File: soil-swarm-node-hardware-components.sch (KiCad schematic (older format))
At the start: 50 parts, among them J1 Conn_ARM_JTAG_SWD_10, J3 BATT_CONN, J4 USB_B_Micro, Q1 DMP3099L-13, Q2 Q_NMOS_GSD, Q3 DMP3099L-13, U3 MCP73812T-420I-OT, X1 32MHz, X2 32,768kHz

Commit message: finalizing 2.0.0
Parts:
- C1, C15, C2, C22, C24, C5: value 100nF -> 100n
- C10, C16, C17, C18: value 4,7µF -> 4.7u
- C11, C7: value 1pF -> 1p
- C12: value 100pF -> 100p
- C13, C14, C19, C20: value 12pF -> 12p
- C21: value 10µF -> 10u
- C23: value 10nF -> 10n
- C3: value 820pF -> 820p
- C6, C8: value 1µF -> 1u
- C9: value 47nF -> 47n
- L1: value 15nH -> 15n
- L2, L4: value 10µH -> 10u
- L3: value 3,9nH -> 3.9n
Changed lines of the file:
@@
 EESchema Schematic File Version 4
-LIBS:power
-LIBS:74xx
 LIBS:soil-swarm-node-hardware-cache
 EELAYER 26 0
@@
 AR Path="/5CDC06D0/5CDCBFD7" Ref="C13"  Part="1"
 F 0 "C13" V 4652 1050 50  0000 C CNN
-F 1 "12pF" V 4561 1050 50  0000 C CNN
+F 1 "12p" V 4561 1050 50  0000 C CNN
 F 2 "Capacitor_SMD:C_0402_1005Metric" H 4438 900 50  0001 C CNN
 F 3 "~" H 4400 1050 50  0001 C CNN
@@
 AR Path="/5CDC06D0/5CDCBFDE" Ref="C14"  Part="1"
 F 0 "C14" V 4652 1450 50  0000 C CNN
-F 1 "12pF" V 4561 1450 50  0000 C CNN
+F 1 "12p" V 4561 1450 50  0000 C CNN
 F 2 "Capacitor_SMD:C_0402_1005Metric" H 4438 1300 50  0001 C CNN
 F 3 "~" H 4400 1450 50  0001 C CNN
@@
 AR Path="/5CDC06D0/5CDCEF68" Ref="C10"  Part="1"
 F 0 "C10" H 8315 1246 50  0000 L CNN
-F 1 "4,7µF" H 8315 1155 50  0000 L CNN
+F 1 "4.7u" H 8315 1155 50  0000 L CNN
 F 2 "Capacitor_SMD:C_0402_1005Metric" H 8238 1050 50  0001 C CNN
 F 3 "~" H 8200 1200 50  0001 C CNN
@@
 AR Path="/5CDC06D0/5CDCEF75" Ref="L1"  Part="1"
 F 0 "L1" H 1753 3746 50  0000 L CNN
-F 1 "15nH" H 1753 3655 50  0000 L CNN
+F 1 "15n" H 1753 3655 50  0000 L CNN
 F 2 "Inductor_SMD:L_0603_1608Metric" H 1700 3700 50  0001 C CNN
 F 3 "~" H 1700 3700 50  0001 C CNN
@@
 AR Path="/5CDC06D0/5CDCEF7C" Ref="L2"  Part="1"
 F 0 "L2" H 1753 4046 50  0000 L CNN
-F 1 "10µH" H 1753 3955 50  0000 L CNN
+F 1 "10u" H 1753 3955 50  0000 L CNN
 F 2 "Inductor_SMD:L_0603_1608Metric" H 1700 4000 50  0001 C CNN
 F 3 "~" H 1700 4000 50  0001 C CNN
@@
 AR Path="/5CDC06D0/5CDCEF8A" Ref="C6"  Part="1"
 F 0 "C6" H 1815 4346 50  0000 L CNN
-F 1 "1µF" H 1815 4255 50  0000 L CNN
+F 1 "1u" H 1815 4255 50  0000 L CNN
 F 2 "Capacitor_SMD:C_0402_1005Metric" H 1738 4150 50  0001 C CNN
 F 3 "~" H 1700 4300 50  0001 C CNN
@@
 AR Path="/5CDC06D0/5CDCEF93" Ref="C9"  Part="1"
 F 0 "C9" H 2215 4346 50  0000 L CNN
-F 1 "47nF" H 2215 4255 50  0000 L CNN
+F 1 "47n" H 2215 4255 50  0000 L CNN
 F 2 "Capacitor_SMD:C_0402_1005Metric" H 2138 4150 50  0001 C CNN
 F 3 "~" H 2100 4300 50  0001 C CNN
@@
 AR Path="/5CDC06D0/5CDCEFA5" Ref="C15"  Part="1"
 F 0 "C15" H 3465 3946 50  0000 L CNN
-F 1 "100nF" H 3465 3855 50  0000 L CNN
+F 1 "100n" H 3465 3855 50  0000 L CNN
 F 2 "Capacitor_SMD:C_0402_1005Metric" H 3388 3750 50  0001 C CNN
 F 3 "~" H 3350 3900 50  0001 C CNN
@@
 AR Path="/5CDC06D0/5CDCEFB2" Ref="C12"  Part="1"
 F 0 "C12" H 2865 3946 50  0000 L CNN
-F 1 "100pF" H 2865 3855 50  0000 L CNN
+F 1 "100p" H 2865 3855 50  0000 L CNN
 F 2 "Capacitor_SMD:C_0402_1005Metric" H 2788 3750 50  0001 C CNN
 F 3 "~" H 2750 3900 50  0001 C CNN
@@
 AR Path="/5CDC06D0/5CDCEFC1" Ref="C3"  Part="1"
 F 0 "C3" H 1165 3696 50  0000 L CNN
-F 1 "820pF" H 1165 3605 50  0000 L CNN
+F 1 "820p" H 1165 3605 50  0000 L CNN
 F 2 "Capacitor_SMD:C_0402_1005Metric" H 1088 3500 50  0001 C CNN
 F 3 "~" H 1050 3650 50  0001 C CNN
@@
 AR Path="/5CDC06D0/5CDCEFD8" Ref="C11"  Part="1"
 F 0 "C11" H 2515 5596 50  0000 L CNN
-F 1 "1pF" H 2515 5505 50  0000 L CNN
+F 1 "1p" H 2515 5505 50  0000 L CNN
 F 2 "Capacitor_SMD:C_0402_1005Metric" H 2438 5400 50  0001 C CNN
 F 3 "~" H 2400 5550 50  0001 C CNN
@@
 AR Path="/5CDC06D0/5CDCEFDF" Ref="C7"  Part="1"
 F 0 "C7" H 1815 5596 50  0000 L CNN
-F 1 "1pF" H 1815 5505 50  0000 L CNN
+F 1 "1p" H 1815 5505 50  0000 L CNN
 F 2 "Capacitor_SMD:C_0402_1005Metric" H 1738 5400 50  0001 C CNN
 F 3 "~" H 1700 5550 50  0001 C CNN
@@
 AR Path="/5CDC06D0/5CDCEFE6" Ref="L3"  Part="1"
 F 0 "L3" V 2240 5400 50  0000 C CNN
-F 1 "3,9nH" V 2149 5400 50  0000 C CNN
+F 1 "3.9n" V 2149 5400 50  0000 C CNN
 F 2 "Inductor_SMD:L_0603_1608Metric" H 2050 5400 50  0001 C CNN
 F 3 "~" H 2050 5400 50  0001 C CNN
@@
 AR Path="/5CDC06D0/5CDCF006" Ref="C8"  Part="1"
 F 0 "C8" H 7915 1246 50  0000 L CNN
-F 1 "1µF" H 7915 1155 50  0000 L CNN
+F 1 "1u" H 7915 1155 50  0000 L CNN
 F 2 "Capacitor_SMD:C_0402_1005Metric" H 7838 1050 50  0001 C CNN
 F 3 "~" H 7800 1200 50  0001 C CNN
@@
 AR Path="/5CDC06D0/5CDCF00D" Ref="C5"  Part="1"
 F 0 "C5" H 7465 1246 50  0000 L CNN
-F 1 "100nF" H 7465 1155 50  0000 L CNN
+F 1 "100n" H 7465 1155 50  0000 L CNN
 F 2 "Capacitor_SMD:C_0402_1005Metric" H 7388 1050 50  0001 C CNN
 F 3 "~" H 7350 1200 50  0001 C CNN
@@
 AR Path="/5CDC06D0/5CDCF014" Ref="C2"  Part="1"
 F 0 "C2" H 7015 1246 50  0000 L CNN
-F 1 "100nF" H 7015 1155 50  0000 L CNN
+F 1 "100n" H 7015 1155 50  0000 L CNN
 F 2 "Capacitor_SMD:C_0402_1005Metric" H 6938 1050 50  0001 C CNN
 F 3 "~" H 6900 1200 50  0001 C CNN
@@
 AR Path="/5CDC06D0/5CDCF01B" Ref="C1"  Part="1"
 F 0 "C1" H 6515 1246 50  0000 L CNN
-F 1 "100nF" H 6515 1155 50  0000 L CNN
+F 1 "100n" H 6515 1155 50  0000 L CNN
 F 2 "Capacitor_SMD:C_0402_1005Metric" H 6438 1050 50  0001 C CNN
 F 3 "~" H 6400 1200 50  0001 C CNN
@@
 AR Path="/5CDC06D0/5CDD4281" Ref="L4"  Part="1"
 F 0 "L4" H 9050 1265 50  0000 C CNN
-F 1 "10µH" H 9050 1174 50  0000 C CNN
+F 1 "10u" H 9050 1174 50  0000 C CNN
 F 2 "Inductor_SMD:L_0603_1608Metric" H 9050 1050 50  0001 C CNN
 F 3 "~" H 9050 1050 50  0001 C CNN
@@
 AR Path="/5CDC06D0/5CDD4288" Ref="C17"  Part="1"
 F 0 "C17" H 6315 2146 50  0000 L CNN
-F 1 "4,7µF" H 6315 2055 50  0000 L CNN
+F 1 "4.7u" H 6315 2055 50  0000 L CNN
 F 2 "Capacitor_SMD:C_0402_1005Metric" H 6238 1950 50  0001 C CNN
 F 3 "~" H 6200 2100 50  0001 C CNN
@@
 AR Path="/5CDC06D0/5CDD429E" Ref="C16"  Part="1"
 F 0 "C16" H 7015 2046 50  0000 L CNN
-F 1 "4,7µF" H 7015 1955 50  0000 L CNN
+F 1 "4.7u" H 7015 1955 50  0000 L CNN
 F 2 "Capacitor_SMD:C_0402_1005Metric" H 6938 1850 50  0001 C CNN
 F 3 "~" H 6900 2000 50  0001 C CNN
@@
 AR Path="/5CDC06D0/5CDD42AB" Ref="C18"  Part="1"
 F 0 "C18" H 8365 2046 50  0000 L CNN
-F 1 "4,7µF" H 8365 1955 50  0000 L CNN
+F 1 "4.7u" H 8365 1955 50  0000 L CNN
 F 2 "Capacitor_SMD:C_0402_1005Metric" H 8288 1850 50  0001 C CNN
 F 3 "~" H 8250 2000 50  0001 C CNN
@@
 AR Path="/5CDC06D0/5CDDAEC5" Ref="C19"  Part="1"
 F 0 "C19" V 4202 2100 50  0000 C CNN
-F 1 "12pF" V 4111 2100 50  0000 C CNN
+F 1 "12p" V 4111 2100 50  0000 C CNN
 F 2 "Capacitor_SMD:C_0402_1005Metric" H 3988 1950 50  0001 C CNN
 F 3 "~" H 3950 2100 50  0001 C CNN
@@
 AR Path="/5CDC06D0/5CDDAECC" Ref="C20"  Part="1"
 F 0 "C20" V 4202 2500 50  0000 C CNN
-F 1 "12pF" V 4111 2500 50  0000 C CNN
+F 1 "12p" V 4111 2500 50  0000 C CNN
 F 2 "Capacitor_SMD:C_0402_1005Metric" H 3988 2350 50  0001 C CNN
 F 3 "~" H 3950 2500 50  0001 C CNN
@@
 AR Path="/5CDC06D0/5CDE0A07" Ref="C21"  Part="1"
 F 0 "C21" H 8915 4596 50  0000 L CNN
-F 1 "10µF" H 8915 4505 50  0000 L CNN
+F 1 "10u" H 8915 4505 50  0000 L CNN
 F 2 "Capacitor_SMD:C_0402_1005Metric" H 8838 4400 50  0001 C CNN
 F 3 "~" H 8800 4550 50  0001 C CNN
@@
 AR Path="/5CDC06D0/5CDE0A0E" Ref="C22"  Part="1"
 F 0 "C22" H 9315 4596 50  0000 L CNN
-F 1 "100nF" H 9315 4505 50  0000 L CNN
+F 1 "100n" H 9315 4505 50  0000 L CNN
 F 2 "Capacitor_SMD:C_0402_1005Metric" H 9238 4400 50  0001 C CNN
 F 3 "~" H 9200 4550 50  0001 C CNN
@@
 AR Path="/5CDC06D0/5CDE0A2F" Ref="C24"  Part="1"
 F 0 "C24" H 10315 3646 50  0000 L CNN
-F 1 "100nF" H 10315 3555 50  0000 L CNN
+F 1 "100n" H 10315 3555 50  0000 L CNN
 F 2 "Capacitor_SMD:C_0402_1005Metric" H 10238 3450 50  0001 C CNN
 F 3 "~" H 10200 3600 50  0001 C CNN
@@
 AR Path="/5CDC06D0/5CDE0A3E" Ref="C23"  Part="1"
 F 0 "C23" H 9815 3646 50  0000 L CNN
-F 1 "10nF" H 9815 3555 50  0000 L CNN
+F 1 "10n" H 9815 3555 50  0000 L CNN
 F 2 "Capacitor_SMD:C_0402_1005Metric" H 9738 3450 50  0001 C CNN
 F 3 "~" H 9700 3600 50  0001 C CNN

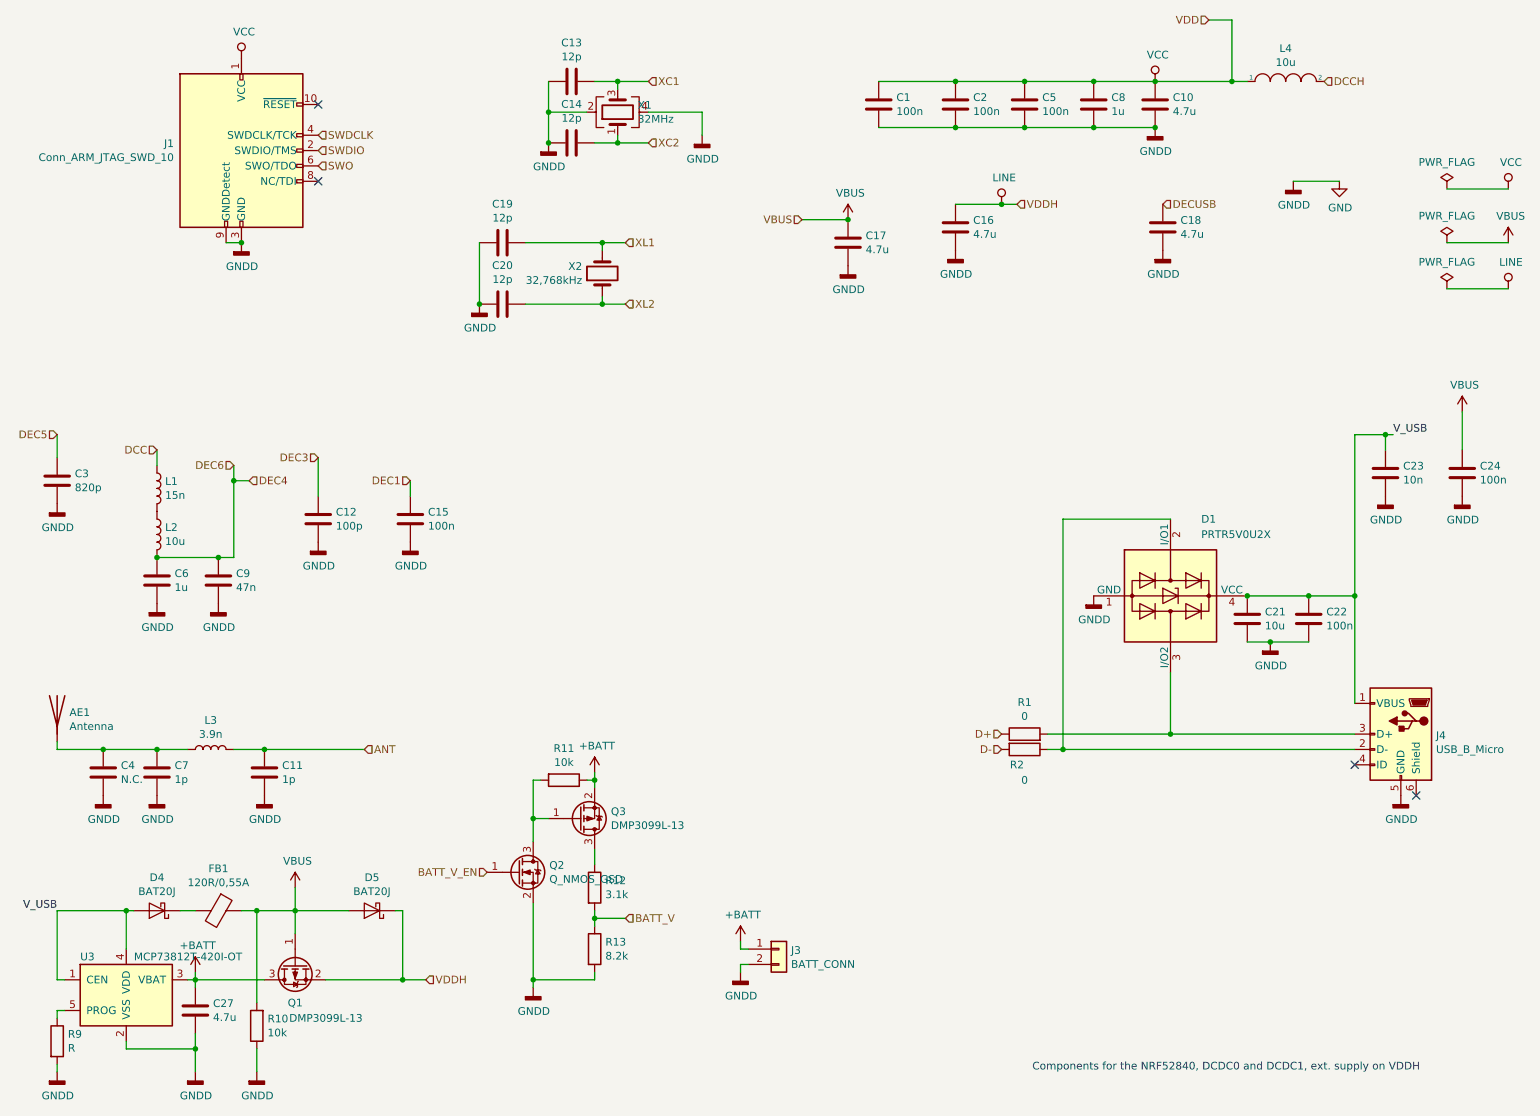
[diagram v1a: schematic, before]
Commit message: update based on Nordic specification
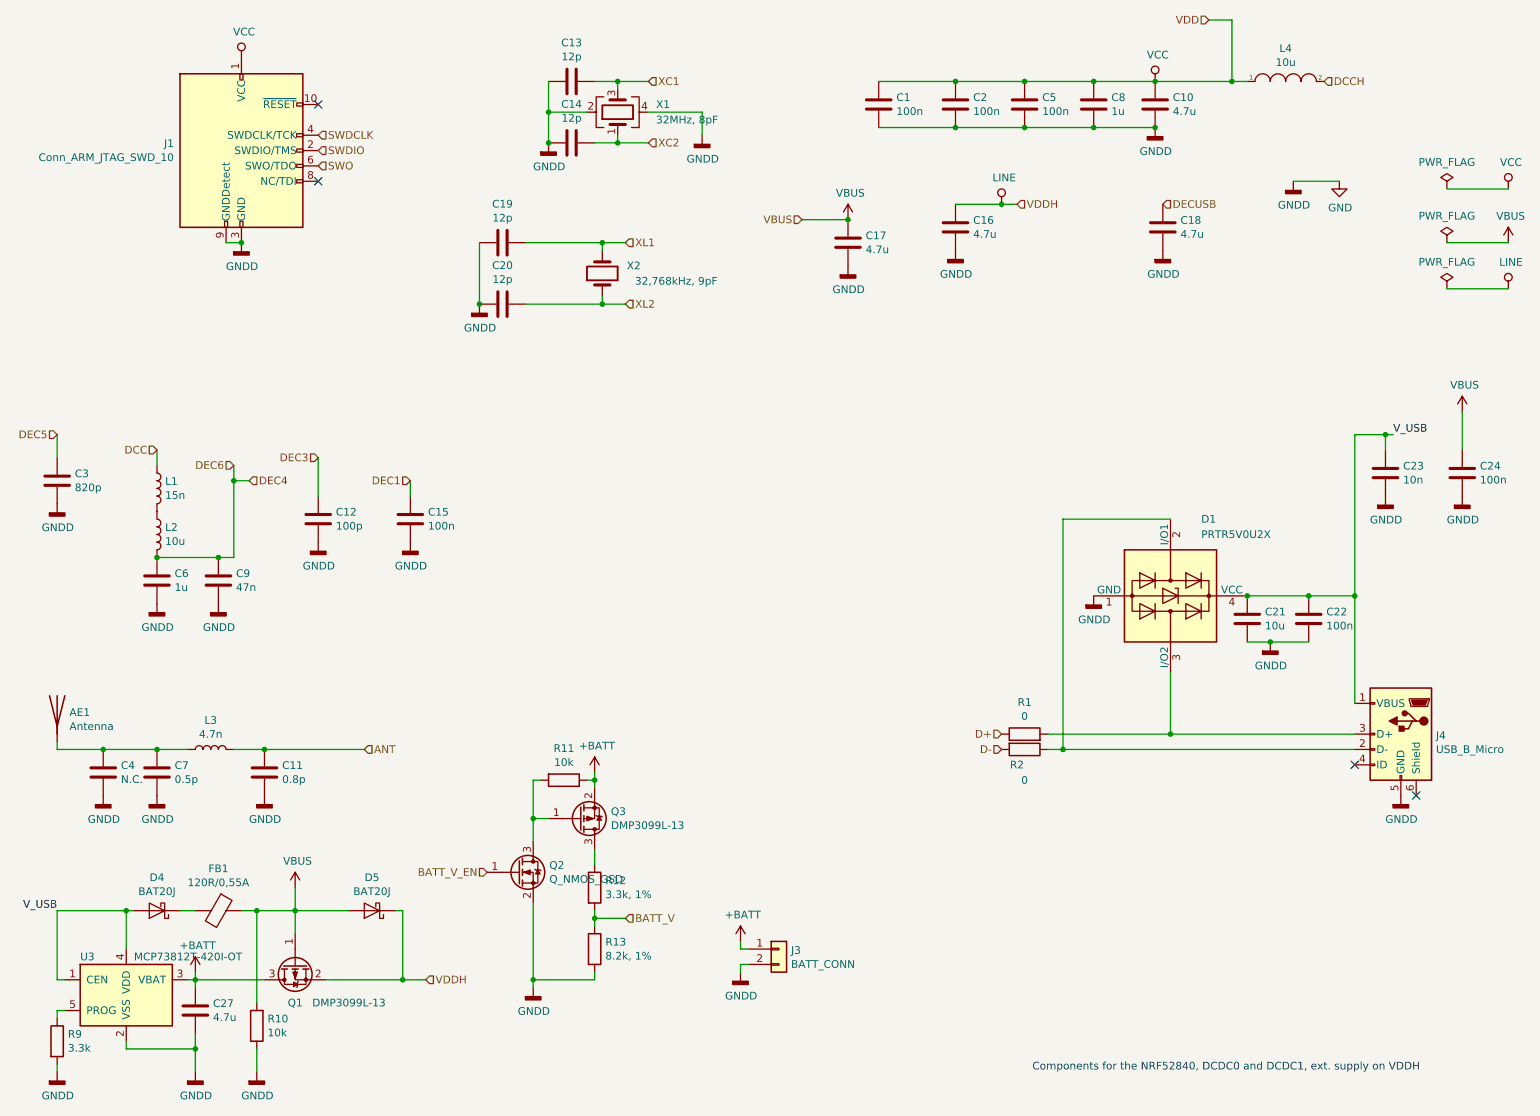
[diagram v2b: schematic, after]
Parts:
- C10, C16, C17, C18, C21, C27, C6, C8: footprint Capacitor_SMD:C_0402_1005Metric -> Capacitor_SMD:C_0603_1608Metric
- C11: value 1p -> 0.8p
- C7: value 1p -> 0.5p
- L1: footprint Inductor_SMD:L_0603_1608Metric -> Inductor_SMD:L_0402_1005Metric
- L3: value 3.9n -> 4.7n; footprint Inductor_SMD:L_0603_1608Metric -> Inductor_SMD:L_0402_1005Metric
- R12: value 3.1k -> 3.3k, 1%
- R13: value 8.2k -> 8.2k, 1%
- R9: value R -> 3.3k
- X1: value 32MHz -> 32MHz, 8pF; footprint Crystal:Crystal_SMD_3225-4Pin_3.2x2.5mm -> Crystal:Crystal_SMD_2016-4Pin_2.0x1.6mm
- X2: value 32,768kHz -> 32,768kHz, 9pF; footprint Crystal:Crystal_SMD_MicroCrystal_CC4V-T1A-2Pin_5.0x1.9mm -> Crystal:Crystal_SMD_3215-2Pin_3.2x1.5mm
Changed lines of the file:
@@
 AR Path="/5CDCBFE5" Ref="X?"  Part="1"
 AR Path="/5CDC06D0/5CDCBFE5" Ref="X1"  Part="1"
-F 0 "X1" V 4746 1119 50  0000 R CNN
-F 1 "32MHz" V 4655 1119 50  0000 R CNN
-F 2 "Crystal:Crystal_SMD_3225-4Pin_3.2x2.5mm" H 4700 1250 50  0001 C CNN
+F 0 "X1" V 4750 1000 50  0000 R CNN
+F 1 "32MHz, 8pF" V 4650 1000 50  0000 R CNN
+F 2 "Crystal:Crystal_SMD_2016-4Pin_2.0x1.6mm" H 4700 1250 50  0001 C CNN
 F 3 "~" H 4700 1250 50  0001 C CNN
 	1    4700 1250
@@
 F 0 "C10" H 8315 1246 50  0000 L CNN
 F 1 "4.7u" H 8315 1155 50  0000 L CNN
-F 2 "Capacitor_SMD:C_0402_1005Metric" H 8238 1050 50  0001 C CNN
+F 2 "Capacitor_SMD:C_0603_1608Metric" H 8238 1050 50  0001 C CNN
 F 3 "~" H 8200 1200 50  0001 C CNN
 	1    8200 1200
@@
 F 0 "L1" H 1753 3746 50  0000 L CNN
 F 1 "15n" H 1753 3655 50  0000 L CNN
-F 2 "Inductor_SMD:L_0603_1608Metric" H 1700 3700 50  0001 C CNN
+F 2 "Inductor_SMD:L_0402_1005Metric" H 1700 3700 50  0001 C CNN
 F 3 "~" H 1700 3700 50  0001 C CNN
 	1    1700 3700
@@
 F 0 "C6" H 1815 4346 50  0000 L CNN
 F 1 "1u" H 1815 4255 50  0000 L CNN
-F 2 "Capacitor_SMD:C_0402_1005Metric" H 1738 4150 50  0001 C CNN
+F 2 "Capacitor_SMD:C_0603_1608Metric" H 1738 4150 50  0001 C CNN
 F 3 "~" H 1700 4300 50  0001 C CNN
 	1    1700 4300
@@
 AR Path="/5CDC06D0/5CDCEFD8" Ref="C11"  Part="1"
 F 0 "C11" H 2515 5596 50  0000 L CNN
-F 1 "1p" H 2515 5505 50  0000 L CNN
+F 1 "0.8p" H 2515 5505 50  0000 L CNN
 F 2 "Capacitor_SMD:C_0402_1005Metric" H 2438 5400 50  0001 C CNN
 F 3 "~" H 2400 5550 50  0001 C CNN
@@
 AR Path="/5CDC06D0/5CDCEFDF" Ref="C7"  Part="1"
 F 0 "C7" H 1815 5596 50  0000 L CNN
-F 1 "1p" H 1815 5505 50  0000 L CNN
+F 1 "0.5p" H 1815 5505 50  0000 L CNN
 F 2 "Capacitor_SMD:C_0402_1005Metric" H 1738 5400 50  0001 C CNN
 F 3 "~" H 1700 5550 50  0001 C CNN
@@
 AR Path="/5CDC06D0/5CDCEFE6" Ref="L3"  Part="1"
 F 0 "L3" V 2240 5400 50  0000 C CNN
-F 1 "3.9n" V 2149 5400 50  0000 C CNN
-F 2 "Inductor_SMD:L_0603_1608Metric" H 2050 5400 50  0001 C CNN
+F 1 "4.7n" V 2149 5400 50  0000 C CNN
+F 2 "Inductor_SMD:L_0402_1005Metric" H 2050 5400 50  0001 C CNN
 F 3 "~" H 2050 5400 50  0001 C CNN
 	1    2050 5400
@@
 F 0 "C8" H 7915 1246 50  0000 L CNN
 F 1 "1u" H 7915 1155 50  0000 L CNN
-F 2 "Capacitor_SMD:C_0402_1005Metric" H 7838 1050 50  0001 C CNN
+F 2 "Capacitor_SMD:C_0603_1608Metric" H 7838 1050 50  0001 C CNN
 F 3 "~" H 7800 1200 50  0001 C CNN
 	1    7800 1200
@@
 F 0 "C17" H 6315 2146 50  0000 L CNN
 F 1 "4.7u" H 6315 2055 50  0000 L CNN
-F 2 "Capacitor_SMD:C_0402_1005Metric" H 6238 1950 50  0001 C CNN
+F 2 "Capacitor_SMD:C_0603_1608Metric" H 6238 1950 50  0001 C CNN
 F 3 "~" H 6200 2100 50  0001 C CNN
 	1    6200 2100
@@
 F 0 "C16" H 7015 2046 50  0000 L CNN
 F 1 "4.7u" H 7015 1955 50  0000 L CNN
-F 2 "Capacitor_SMD:C_0402_1005Metric" H 6938 1850 50  0001 C CNN
+F 2 "Capacitor_SMD:C_0603_1608Metric" H 6938 1850 50  0001 C CNN
 F 3 "~" H 6900 2000 50  0001 C CNN
 	1    6900 2000
@@
 F 0 "C18" H 8365 2046 50  0000 L CNN
 F 1 "4.7u" H 8365 1955 50  0000 L CNN
-F 2 "Capacitor_SMD:C_0402_1005Metric" H 8288 1850 50  0001 C CNN
+F 2 "Capacitor_SMD:C_0603_1608Metric" H 8288 1850 50  0001 C CNN
 F 3 "~" H 8250 2000 50  0001 C CNN
 	1    8250 2000
@@
 AR Path="/5CDDAED3" Ref="X?"  Part="1"
 AR Path="/5CDC06D0/5CDDAED3" Ref="X2"  Part="1"
-F 0 "X2" V 4646 2431 50  0000 L CNN
-F 1 "32,768kHz" V 4555 2431 50  0000 L CNN
-F 2 "Crystal:Crystal_SMD_MicroCrystal_CC4V-T1A-2Pin_5.0x1.9mm" H 4600 2300 50  0001 C CNN
+F 0 "X2" V 4650 2050 50  0000 L CNN
+F 1 "32,768kHz, 9pF" V 4550 1550 50  0000 L CNN
+F 2 "Crystal:Crystal_SMD_3215-2Pin_3.2x1.5mm" H 4600 2300 50  0001 C CNN
 F 3 "~" H 4600 2300 50  0001 C CNN
 	1    4600 2300
@@
 F 0 "C21" H 8915 4596 50  0000 L CNN
 F 1 "10u" H 8915 4505 50  0000 L CNN
-F 2 "Capacitor_SMD:C_0402_1005Metric" H 8838 4400 50  0001 C CNN
+F 2 "Capacitor_SMD:C_0603_1608Metric" H 8838 4400 50  0001 C CNN
 F 3 "~" H 8800 4550 50  0001 C CNN
 	1    8800 4550
@@
 F 0 "C27" H 2065 7146 50  0000 L CNN
 F 1 "4.7u" H 2065 7055 50  0000 L CNN
-F 2 "Capacitor_SMD:C_0402_1005Metric" H 1988 6950 50  0001 C CNN
+F 2 "Capacitor_SMD:C_0603_1608Metric" H 1988 6950 50  0001 C CNN
 F 3 "~" H 1950 7100 50  0001 C CNN
 	1    1950 7100
@@
 P 1050 7300
 F 0 "R9" H 1120 7346 50  0000 L CNN
-F 1 "R" H 1120 7255 50  0000 L CNN
+F 1 "3.3k" H 1120 7255 50  0000 L CNN
 F 2 "Resistor_SMD:R_0402_1005Metric" V 980 7300 50  0001 C CNN
 F 3 "~" H 1050 7300 50  0001 C CNN
@@
 P 2600 6800
 F 0 "Q1" V 2850 6800 50  0000 C CNN
-F 1 "DMP3099L-13" V 2950 6600 50  0000 C CNN
+F 1 "DMP3099L-13" V 2850 6450 50  0000 C CNN
 F 2 "Package_TO_SOT_SMD:SOT-23" H 2800 6900 50  0001 C CNN
 F 3 "~" H 2600 6800 50  0001 C CNN
@@
 P 4550 6300
 F 0 "R12" H 4620 6346 50  0000 L CNN
-F 1 "3.1k" H 4620 6255 50  0000 L CNN
+F 1 "3.3k, 1%" H 4620 6255 50  0000 L CNN
 F 2 "Resistor_SMD:R_0402_1005Metric" V 4480 6300 50  0001 C CNN
 F 3 "~" H 4550 6300 50  0001 C CNN
@@
 P 4550 6700
 F 0 "R13" H 4620 6746 50  0000 L CNN
-F 1 "8.2k" H 4620 6655 50  0000 L CNN
+F 1 "8.2k, 1%" H 4620 6655 50  0000 L CNN
 F 2 "Resistor_SMD:R_0402_1005Metric" V 4480 6700 50  0001 C CNN
 F 3 "~" H 4550 6700 50  0001 C CNN

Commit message: update schematic
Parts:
- D1: symbol Power_Protection:PRTR5V0U2X -> soil-swarm-node-hardware-rescue:PRTR5V0U2X-Power_Protection
- J1: symbol Connector:Conn_ARM_JTAG_SWD_10 -> soil-swarm-node-hardware-rescue:Conn_ARM_JTAG_SWD_10-Connector
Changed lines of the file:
@@
 $EndDescr
 $Comp
-L Connector:Conn_ARM_JTAG_SWD_10 J?
+L soil-swarm-node-hardware-rescue:Conn_ARM_JTAG_SWD_10-Connector J?
 U 1 1 5CDC6ACC
 P 2250 1500
@@
 $EndComp
 $Comp
-L Power_Protection:PRTR5V0U2X D?
+L soil-swarm-node-hardware-rescue:PRTR5V0U2X-Power_Protection D?
 U 1 1 5CDE09E9
 P 8300 4400
